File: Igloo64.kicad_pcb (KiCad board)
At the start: 2 copper layers, 83.8 x 90.2 mm, 7 parts, among them J1 Conn_02x32_Counter_Clockwise, J2 Conn_01x16, J3 Conn_01x16, J4 Conn_01x16, J5 Conn_01x16, J6 Conn_02x32_Odd_Even, J7 Conn_02x32_Odd_Even

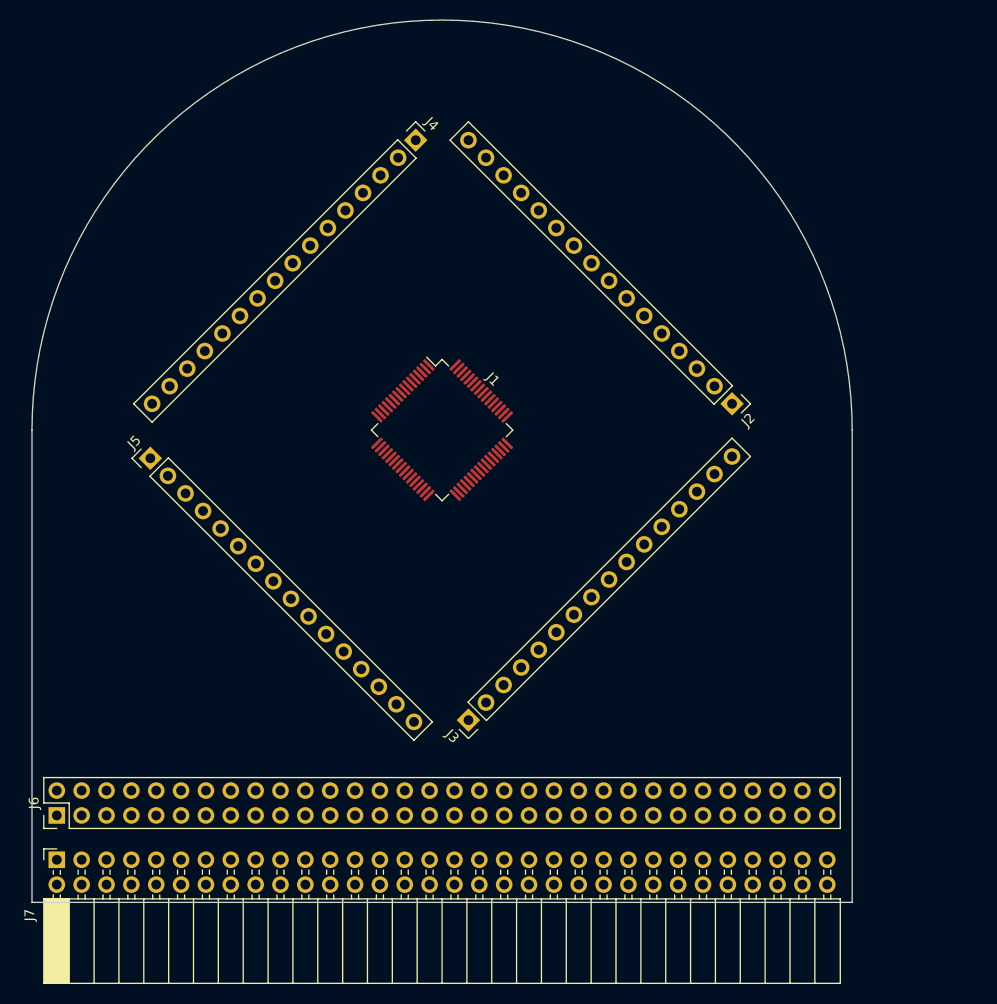
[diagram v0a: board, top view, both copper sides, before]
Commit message: Finish wiring of buses.
Also rotate TQFP footprint temporarily and move headers closer to it. Add tracks from TQFP to header on one side only to see how well it can be routed.
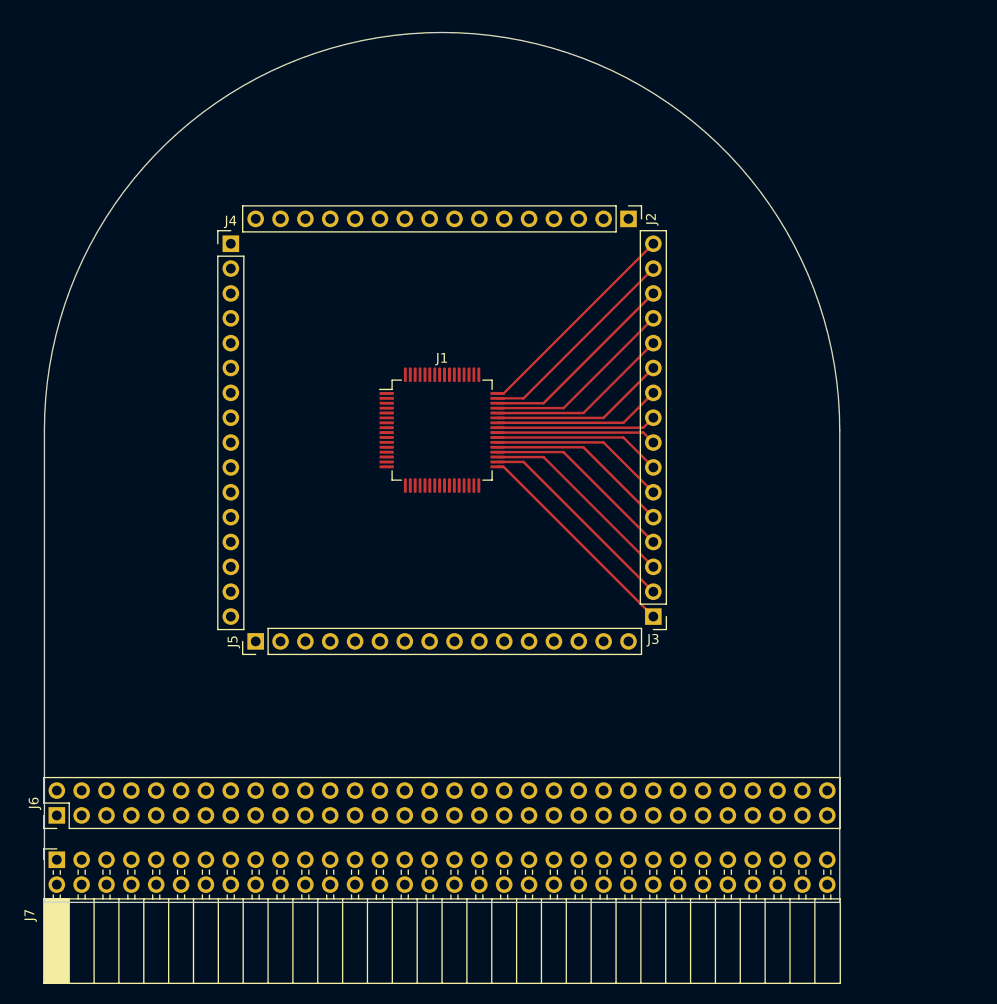
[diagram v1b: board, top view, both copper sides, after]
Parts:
- moved J2 21.7 mm to (151.1, 67.3), turned to -90 degrees
- moved J4 21.7 mm to (110.5, 69.8), turned to 0 degrees
- moved J3 21.7 mm to (153.7, 108.0), turned to 180 degrees
- moved J5 21.6 mm to (113.0, 110.5), turned to 90 degrees
- turned J1 to 0 degrees
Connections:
- J6 pad 10: unconnected-(J6-Pad10) -> /pin60
- J6 pad 11: unconnected-(J6-Pad11) -> /pin6
- J6 pad 12: unconnected-(J6-Pad12) -> /pin59
- J6 pad 13: unconnected-(J6-Pad13) -> /pin7
- J6 pad 14: unconnected-(J6-Pad14) -> /pin58
- J6 pad 15: unconnected-(J6-Pad15) -> /pin8
- J6 pad 16: unconnected-(J6-Pad16) -> /pin57
- J6 pad 17: unconnected-(J6-Pad17) -> /pin9
- J6 pad 18: unconnected-(J6-Pad18) -> /pin56
- J6 pad 19: unconnected-(J6-Pad19) -> /pin10
- J6 pad 20: unconnected-(J6-Pad20) -> /pin55
- J6 pad 21: unconnected-(J6-Pad21) -> /pin11
- J6 pad 22: unconnected-(J6-Pad22) -> /pin54
- J6 pad 23: unconnected-(J6-Pad23) -> /pin12
- J6 pad 24: unconnected-(J6-Pad24) -> /pin53
- J6 pad 25: unconnected-(J6-Pad25) -> /pin13
- J6 pad 26: unconnected-(J6-Pad26) -> /pin52
- J6 pad 28: unconnected-(J6-Pad28) -> /pin51
- J6 pad 30: unconnected-(J6-Pad30) -> /pin50
- J6 pad 39: unconnected-(J6-Pad39) -> /pin20
- J6 pad 41: unconnected-(J6-Pad41) -> /pin21
- J6 pad 43: unconnected-(J6-Pad43) -> /pin22
- J6 pad 45: unconnected-(J6-Pad45) -> /pin23
- J6 pad 47: unconnected-(J6-Pad47) -> /pin24
- J6 pad 49: unconnected-(J6-Pad49) -> /pin25
- J6 pad 51: unconnected-(J6-Pad51) -> /pin26
- J6 pad 53: unconnected-(J6-Pad53) -> /pin27
- J6 pad 55: unconnected-(J6-Pad55) -> /pin28
- J6 pad 9: unconnected-(J6-Pad9) -> /pin5
- J7 pad 10: unconnected-(J7-Pad10) -> /pin60
- J7 pad 11: unconnected-(J7-Pad11) -> /pin6
- J7 pad 12: unconnected-(J7-Pad12) -> /pin59
- J7 pad 13: unconnected-(J7-Pad13) -> /pin7
- J7 pad 14: unconnected-(J7-Pad14) -> /pin58
- J7 pad 15: unconnected-(J7-Pad15) -> /pin8
- J7 pad 16: unconnected-(J7-Pad16) -> /pin57
- J7 pad 17: unconnected-(J7-Pad17) -> /pin9
- J7 pad 18: unconnected-(J7-Pad18) -> /pin56
- J7 pad 19: unconnected-(J7-Pad19) -> /pin10
- J7 pad 20: unconnected-(J7-Pad20) -> /pin55
- J7 pad 21: unconnected-(J7-Pad21) -> /pin11
- J7 pad 22: unconnected-(J7-Pad22) -> /pin54
- J7 pad 23: unconnected-(J7-Pad23) -> /pin12
- J7 pad 24: unconnected-(J7-Pad24) -> /pin53
- J7 pad 25: unconnected-(J7-Pad25) -> /pin13
- J7 pad 26: unconnected-(J7-Pad26) -> /pin52
- J7 pad 28: unconnected-(J7-Pad28) -> /pin51
- J7 pad 30: unconnected-(J7-Pad30) -> /pin50
- J7 pad 32: unconnected-(J7-Pad32) -> /pin49
- J7 pad 34: unconnected-(J7-Pad34) -> /pin48
- J7 pad 36: unconnected-(J7-Pad36) -> /pin47
- J7 pad 38: unconnected-(J7-Pad38) -> /pin46
- J7 pad 39: unconnected-(J7-Pad39) -> /pin20
- J7 pad 40: unconnected-(J7-Pad40) -> /pin45
- J7 pad 41: unconnected-(J7-Pad41) -> /pin21
- J7 pad 42: unconnected-(J7-Pad42) -> /pin44
- J7 pad 43: unconnected-(J7-Pad43) -> /pin22
- J7 pad 44: unconnected-(J7-Pad44) -> /pin43
- J7 pad 45: unconnected-(J7-Pad45) -> /pin23
- J7 pad 46: unconnected-(J7-Pad46) -> /pin42
- J7 pad 47: unconnected-(J7-Pad47) -> /pin24
- J7 pad 48: unconnected-(J7-Pad48) -> /pin41
- J7 pad 49: unconnected-(J7-Pad49) -> /pin25
- J7 pad 50: unconnected-(J7-Pad50) -> /pin40
- J7 pad 51: unconnected-(J7-Pad51) -> /pin26
- J7 pad 52: unconnected-(J7-Pad52) -> /pin39
- J7 pad 53: unconnected-(J7-Pad53) -> /pin27
- J7 pad 54: unconnected-(J7-Pad54) -> /pin38
- J7 pad 55: unconnected-(J7-Pad55) -> /pin28
- J7 pad 56: unconnected-(J7-Pad56) -> /pin37
- J7 pad 57: unconnected-(J7-Pad57) -> /pin29
- J7 pad 58: unconnected-(J7-Pad58) -> /pin36
- J7 pad 59: unconnected-(J7-Pad59) -> /pin30
- J7 pad 60: unconnected-(J7-Pad60) -> /pin35
- J7 pad 61: unconnected-(J7-Pad61) -> /pin31
- J7 pad 62: unconnected-(J7-Pad62) -> /pin34
- J7 pad 63: unconnected-(J7-Pad63) -> /pin32
- J7 pad 64: unconnected-(J7-Pad64) -> /pin33
- J7 pad 9: unconnected-(J7-Pad9) -> /pin5
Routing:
- net /pin48: track 0.00 -> 22.3 mm
- net /pin33: track 0.00 -> 22.3 mm
- net /pin47: track 0.00 -> 21.4 mm
- net /pin34: track 0.00 -> 21.4 mm
- net /pin46: track 0.00 -> 20.6 mm
- net /pin35: track 0.00 -> 20.6 mm
- net /pin45: track 0.00 -> 19.7 mm
- net /pin36: track 0.00 -> 19.7 mm
- net /pin44: track 0.00 -> 18.9 mm
- net /pin37: track 0.00 -> 18.9 mm
- net /pin43: track 0.00 -> 18.0 mm
- net /pin38: track 0.00 -> 18.0 mm
- net /pin42: track 0.00 -> 17.2 mm
- net /pin39: track 0.00 -> 17.2 mm
- net /pin41: track 0.00 -> 16.3 mm
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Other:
- board size 83.8 x 90.2 mm -> 81.3 x 88.9 mm

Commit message: Add secondary PCB and double up connectors.
The secondary PCB plugs into the solderless breadboard in the same way as a 64-pin DIL chip (0.3in width). It's just connectors. Also make the ring of connectors around the TQFP footprint into 2-row parts. You can never have too many connection points.
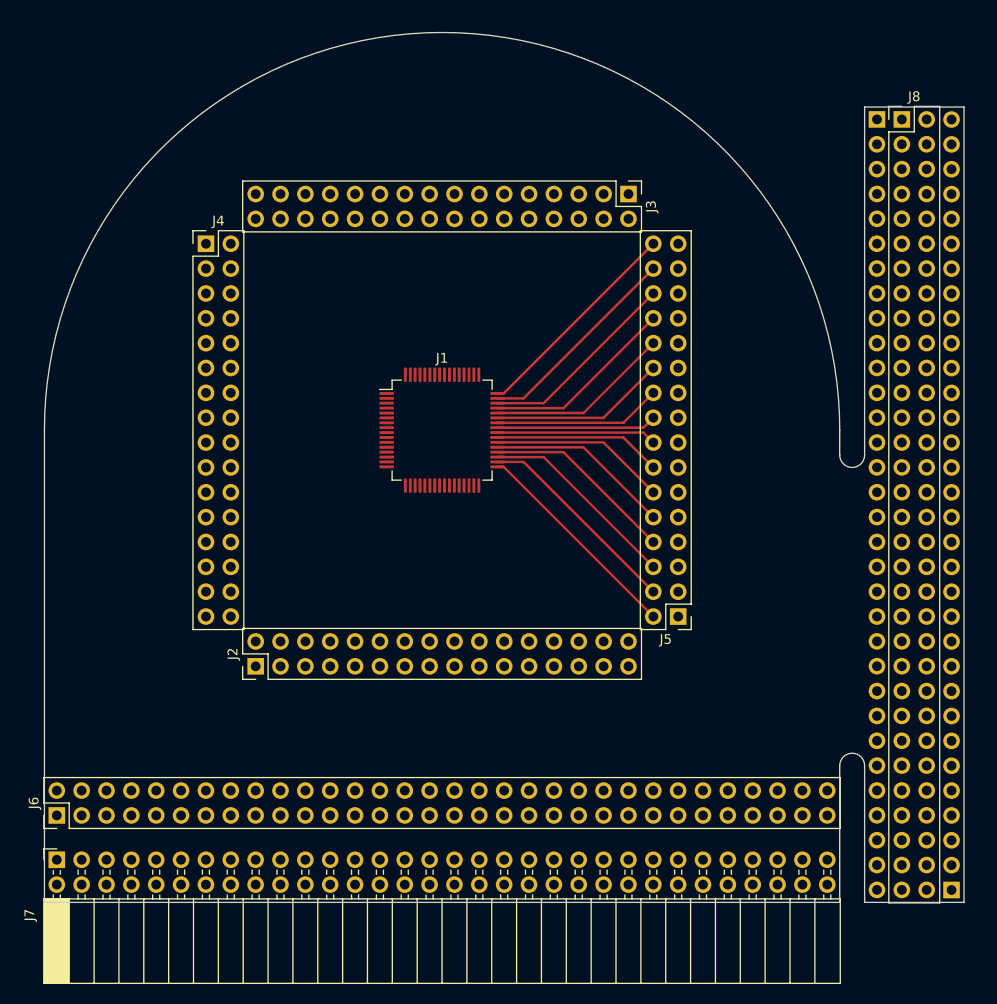
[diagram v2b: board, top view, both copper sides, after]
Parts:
- added J10: Conn_01x32, Connector_PinHeader_2.54mm:PinHeader_1x32_P2.54mm_Vertical, B.Cu at (184.1, 135.9)
- added J8: Conn_02x32_Odd_Even, Connector_PinHeader_2.54mm:PinHeader_2x32_P2.54mm_Vertical, F.Cu at (179.1, 57.1)
- added J9: Conn_01x32, Connector_PinHeader_2.54mm:PinHeader_1x32_P2.54mm_Vertical, B.Cu at (176.5, 57.1)
- J2, J3, J4, J5: value Conn_01x16 -> Conn_02x16_Odd_Even; footprint Connector_PinHeader_2.54mm:PinHeader_1x16_P2.54mm_Vertical -> Connector_PinHeader_2.54mm:PinHeader_2x16_P2.54mm_Vertical
- moved J2 59.5 mm to (113.0, 113.0), turned to 90 degrees
- moved J3 43.3 mm to (151.1, 64.8), turned to -90 degrees
- moved J5 43.3 mm to (156.2, 108.0), turned to 180 degrees
- moved J4 2.54 mm to (108.0, 69.8)
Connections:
- J2 pad 1: /pin49 -> /pin17
- J2 pad 10: /pin58 -> /pin21
- J2 pad 11: /pin59 -> /pin22
- J2 pad 12: /pin60 -> /pin22
- J2 pad 13: /pin61 -> /pin23
- J2 pad 14: /pin62 -> /pin23
- J2 pad 15: /pin63 -> /pin24
- J2 pad 16: /pin64 -> /pin24
- J2 pad 2: /pin50 -> /pin17
- J2 pad 3: /pin51 -> /pin18
- J2 pad 4: /pin52 -> /pin18
- J2 pad 5: /pin53 -> /pin19
- J2 pad 6: /pin54 -> /pin19
- J2 pad 7: /pin55 -> /pin20
- J2 pad 8: /pin56 -> /pin20
- J2 pad 9: /pin57 -> /pin21
- J3 pad 1: /pin33 -> /pin49
- J3 pad 10: /pin42 -> /pin53
- J3 pad 11: /pin43 -> /pin54
- J3 pad 12: /pin44 -> /pin54
- J3 pad 13: /pin45 -> /pin55
- J3 pad 14: /pin46 -> /pin55
- J3 pad 15: /pin47 -> /pin56
- J3 pad 16: /pin48 -> /pin56
- J3 pad 2: /pin34 -> /pin49
- J3 pad 3: /pin35 -> /pin50
- J3 pad 4: /pin36 -> /pin50
- J3 pad 5: /pin37 -> /pin51
- J3 pad 6: /pin38 -> /pin51
- J3 pad 7: /pin39 -> /pin52
- J3 pad 8: /pin40 -> /pin52
- J3 pad 9: /pin41 -> /pin53
- J4 pad 10: /pin10 -> /pin5
- J4 pad 11: /pin11 -> /pin6
- J4 pad 12: /pin12 -> /pin6
- J4 pad 13: /pin13 -> /pin7
- J4 pad 14: /pin14 -> /pin7
- J4 pad 15: /pin15 -> /pin8
- J4 pad 16: /pin16 -> /pin8
- J4 pad 2: /pin2 -> /pin1
- J4 pad 3: /pin3 -> /pin2
- J4 pad 4: /pin4 -> /pin2
- J4 pad 5: /pin5 -> /pin3
- J4 pad 6: /pin6 -> /pin3
- J4 pad 7: /pin7 -> /pin4
- J4 pad 8: /pin8 -> /pin4
- J4 pad 9: /pin9 -> /pin5
- J5 pad 1: /pin17 -> /pin33
- J5 pad 10: /pin26 -> /pin37
- J5 pad 11: /pin27 -> /pin38
- J5 pad 12: /pin28 -> /pin38
- J5 pad 13: /pin29 -> /pin39
- J5 pad 14: /pin30 -> /pin39
- J5 pad 15: /pin31 -> /pin40
- J5 pad 16: /pin32 -> /pin40
- J5 pad 2: /pin18 -> /pin33
- J5 pad 3: /pin19 -> /pin34
- J5 pad 4: /pin20 -> /pin34
- J5 pad 5: /pin21 -> /pin35
- J5 pad 6: /pin22 -> /pin35
- J5 pad 7: /pin23 -> /pin36
- J5 pad 8: /pin24 -> /pin36
- J5 pad 9: /pin25 -> /pin37
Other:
- board size 81.3 x 88.9 mm -> 94 x 88.9 mm

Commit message: Rotate TQFP and route all tracks.
But I had to make the board wider to allow the tracks near J6 and J7 to be routed. Some rear tracks still a bit uneven and asymmetrical. Needs proper mouse bites.
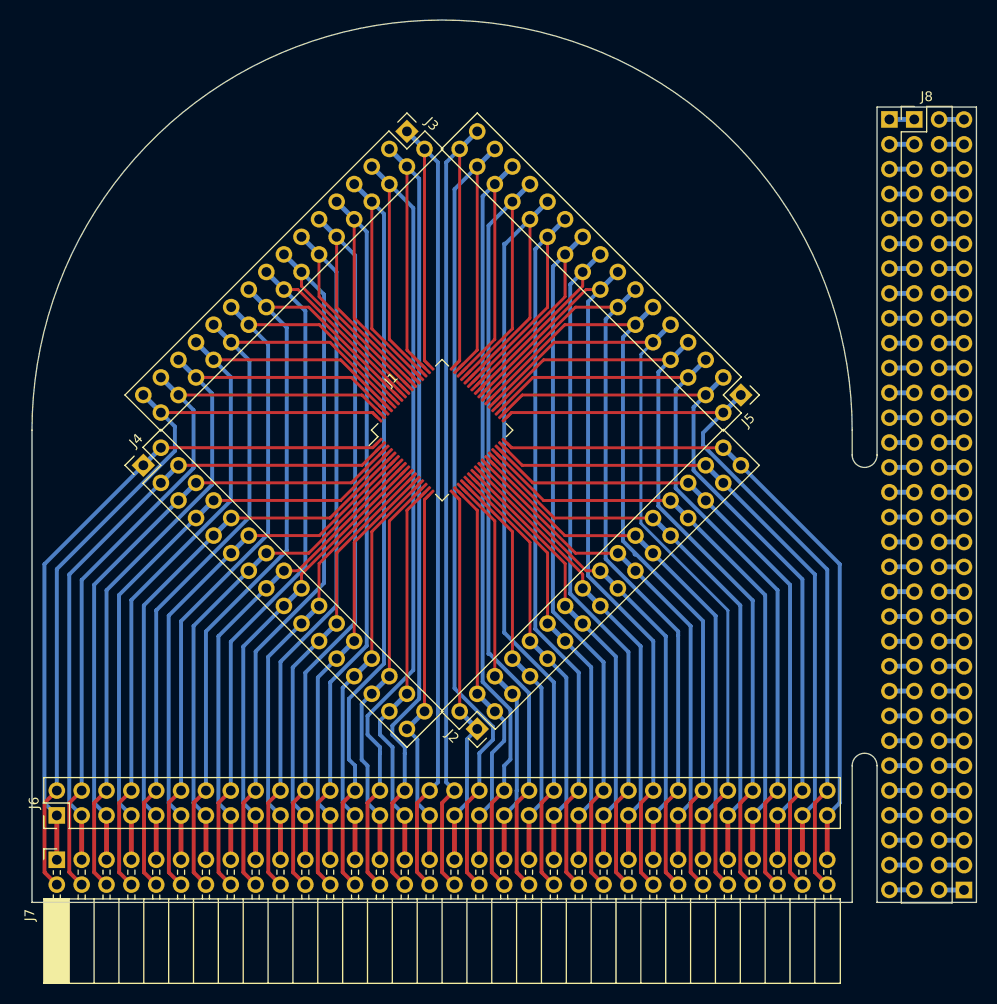
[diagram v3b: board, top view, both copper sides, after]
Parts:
- moved J2 23.5 mm to (135.7, 119.4), turned to 135 degrees
- moved J4 23.5 mm to (101.5, 92.5), turned to 45 degrees
- moved J5 23.5 mm to (162.6, 85.3), turned to -135 degrees
- moved J3 23.5 mm to (128.5, 58.4), turned to -45 degrees
- moved J8 1.27 mm to (180.3, 57.1)
- moved J10 1.27 mm to (185.4, 135.9)
- moved J9 1.27 mm to (177.8, 57.1)
- turned J1 to 45 degrees
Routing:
- net /pin49: track 0.00 -> 102.5 mm
- net /pin50: track 0.00 -> 100.6 mm
- net /pin51: track 0.00 -> 99.2 mm
- net /pin52: track 0.00 -> 95.4 mm
- net /pin53: track 0.00 -> 92.5 mm
- net /pin54: track 0.00 -> 90.7 mm
- net /pin55: track 0.00 -> 88.3 mm
- net /pin56: track 0.00 -> 86.4 mm
- net /pin57: track 0.00 -> 84.8 mm
- net /pin58: track 0.00 -> 84.1 mm
- net /pin59: track 0.00 -> 83.3 mm
- net /pin60: track 0.00 -> 82.6 mm
- net /pin61: track 0.00 -> 81.9 mm
- net /pin62: track 0.00 -> 81.2 mm
- net /pin63: track 0.00 -> 80.4 mm
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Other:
- board size 94 x 88.9 mm -> 96.5 x 90.2 mm
